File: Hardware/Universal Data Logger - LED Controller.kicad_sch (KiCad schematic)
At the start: 0 parts

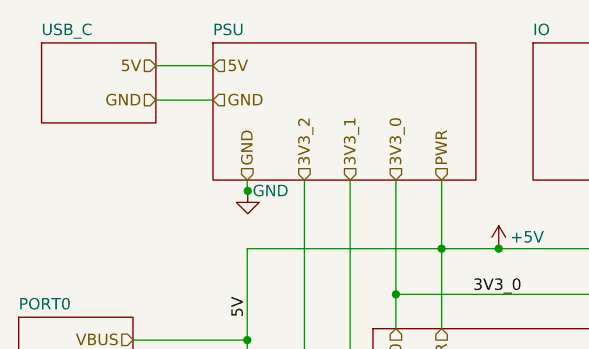
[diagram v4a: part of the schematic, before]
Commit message: added boost converter and shared power
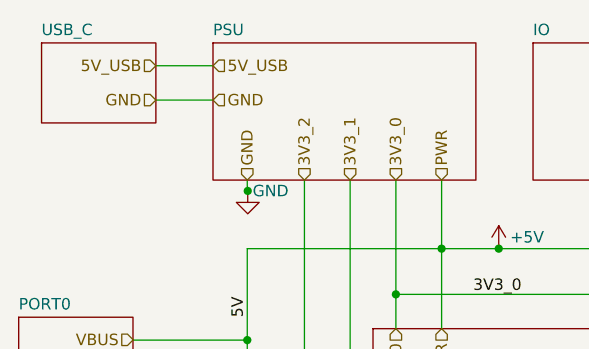
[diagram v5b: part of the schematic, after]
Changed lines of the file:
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@@
     (effects (font (size 1.27 1.27)) (justify left))
-  )
-  (hierarchical_label "5V" (shape input) (at 109.22 43.18 180)
-    (effects (font (size 1.27 1.27)) (justify right))
   )
   (hierarchical_label "3V3_0" (shape input) (at 135.89 72.39 270)
@@
     (effects (font (size 1.27 1.27)) (justify right))
   )
-  (hierarchical_label "5V" (shape input) (at 115.57 43.18 0)
+  (hierarchical_label "5V_USB" (shape input) (at 115.57 43.18 0)
     (effects (font (size 1.27 1.27)) (justify left))
   )
@@
   (hierarchical_label "3V3_0" (shape input) (at 135.89 55.88 90)
     (effects (font (size 1.27 1.27)) (justify left))
+  )
+  (hierarchical_label "5V_USB" (shape input) (at 109.22 43.18 180)
+    (effects (font (size 1.27 1.27)) (justify right))
   )
   (hierarchical_label "I2C_0" (shape input) (at 106.68 96.52 180)
@@
       (reference "#PWR?") (unit 1) (value "GND") (footprint "")
     )
+    (path "/de536fb9-bd34-41b3-aa78-3b4ee3eb44c1/816e4c72-e10d-4109-92a5-908b846ac521"
+      (reference "#PWR?") (unit 1) (value "GND") (footprint "")
+    )
     (path "/7725ee63-5a52-4ce3-8509-bb9f639adcfa/89bff7d1-eb89-4467-abd1-c6203a55d334"
       (reference "#PWR?") (unit 1) (value "~") (footprint "")
@@
       (reference "#PWR?") (unit 1) (value "GND") (footprint "")
     )
+    (path "/de536fb9-bd34-41b3-aa78-3b4ee3eb44c1/e616355e-b9c7-466d-8d6b-f6372f5c9430"
+      (reference "#PWR?") (unit 1) (value "GND") (footprint "")
+    )
     (path "/ed8d3444-b973-4b23-b52f-30b61ef22ad3"
       (reference "#PWR?") (unit 1) (value "GND") (footprint "")
@@
       (reference "#PWR?") (unit 1) (value "~") (footprint "")
     )
+    (path "/0b401b8f-2393-4525-bdd9-a0e4dc05fd07/f296a7f9-6705-4446-8a68-6cdcf5f6b1e7"
+      (reference "#PWR?") (unit 1) (value "~") (footprint "")
+    )
     (path "/416a6167-b792-4f97-9743-b5ec01ae5243/f296a7f9-6705-4446-8a68-6cdcf5f6b1e7"
-      (reference "#PWR?") (unit 1) (value "~") (footprint "")
-    )
-    (path "/0b401b8f-2393-4525-bdd9-a0e4dc05fd07/f296a7f9-6705-4446-8a68-6cdcf5f6b1e7"
       (reference "#PWR?") (unit 1) (value "~") (footprint "")
     )
@@
       (reference "C?") (unit 1) (value "10u") (footprint "")
     )
+    (path "/de536fb9-bd34-41b3-aa78-3b4ee3eb44c1/1aeb5f5f-cdff-4997-9c39-bf9eb003ca01"
+      (reference "C?") (unit 1) (value "1u") (footprint "")
+    )
+    (path "/de536fb9-bd34-41b3-aa78-3b4ee3eb44c1/1f3f4a2b-ad4c-4cfc-b60f-53aa9a5a4963"
+      (reference "C?") (unit 1) (value "10u") (footprint "")
+    )
     (path "/7c624ac6-450b-40ca-801e-524e011fb28e/31a2d955-d31f-4da0-8acb-4b0674a9da0a"
       (reference "C?") (unit 1) (value "4.7u") (footprint "")
     )
+    (path "/de536fb9-bd34-41b3-aa78-3b4ee3eb44c1/3a81c65e-eb89-462a-bf3f-509d8f776024"
+      (reference "C?") (unit 1) (value "4.7u") (footprint "")
+    )
     (path "/9782f829-68cb-4687-94a0-b365f380bc5e/3f06b84e-e0ff-4f8c-998d-4e1f029dcf28"
       (reference "C?") (unit 1) (value "10nF") (footprint "Capacitor_SMD:C_0805_2012Metric_Pad1.15x1.40mm_HandSolder")
@@
       (reference "C?") (unit 1) (value "10nF") (footprint "Capacitor_SMD:C_0805_2012Metric_Pad1.15x1.40mm_HandSolder")
     )
+    (path "/de536fb9-bd34-41b3-aa78-3b4ee3eb44c1/d2b1c201-3aa4-4a10-926d-482ef8e79ac4"
+      (reference "C?") (unit 1) (value "4.7u") (footprint "")
+    )
     (path "/de536fb9-bd34-41b3-aa78-3b4ee3eb44c1/d5744843-7628-4379-ab5c-db9cb496570f"
       (reference "C?") (unit 1) (value "10u") (footprint "")
@@
       (reference "D?") (unit 1) (value "GLED") (footprint "")
     )
+    (path "/de536fb9-bd34-41b3-aa78-3b4ee3eb44c1/625ae2c4-5527-4512-8d4e-2af0785a4a51"
+      (reference "D?") (unit 1) (value "15MQ 040NTR") (footprint "")
+    )
     (path "/9f024182-f9b7-433c-babf-5bba7b2290ff/c65fc7ad-c5d7-4502-ab26-6038cc997284"
       (reference "D?") (unit 1) (value "~") (footprint "")
@@
       (reference "J?") (unit 1) (value "~") (footprint "")
     )
+    (path "/416a6167-b792-4f97-9743-b5ec01ae5243/365bbbd0-ace9-4e3f-a9ec-01ed49158099"
+      (reference "J?") (unit 1) (value "~") (footprint "")
+    )
     (path "/0b401b8f-2393-4525-bdd9-a0e4dc05fd07/365bbbd0-ace9-4e3f-a9ec-01ed49158099"
       (reference "J?") (unit 1) (value "~") (footprint "")
     )
-    (path "/416a6167-b792-4f97-9743-b5ec01ae5243/365bbbd0-ace9-4e3f-a9ec-01ed49158099"
-      (reference "J?") (unit 1) (value "~") (footprint "")
+    (path "/de536fb9-bd34-41b3-aa78-3b4ee3eb44c1/9d457abc-74ee-43b4-89ec-b5a19bd46e46"
+      (reference "J?") (unit 1) (value "Bat_conn") (footprint "")
     )
     (path "/aa6de945-d617-4c34-aaed-6b2511874162/baf5ed95-c1f0-4125-a1c7-86f2d1455922"
@@
       (reference "L?") (unit 1) (value "BLM21PG 221") (footprint "")
     )
+    (path "/de536fb9-bd34-41b3-aa78-3b4ee3eb44c1/ff82fc8e-d594-45e1-9241-bbd7809e4925"
+      (reference "L?") (unit 1) (value "L-1616FPS 10uH") (footprint "")
+    )
+    (path "/0b401b8f-2393-4525-bdd9-a0e4dc05fd07/12f23d58-6cd8-4e91-9a7a-e2dde86f8cdc"
+      (reference "Q?") (unit 1) (value "SI4776DY-GE3") (footprint "")
+    )
     (path "/416a6167-b792-4f97-9743-b5ec01ae5243/12f23d58-6cd8-4e91-9a7a-e2dde86f8cdc"
       (reference "Q?") (unit 1) (value "SI4776DY-GE3") (footprint "")
     )
-    (path "/0b401b8f-2393-4525-bdd9-a0e4dc05fd07/12f23d58-6cd8-4e91-9a7a-e2dde86f8cdc"
-      (reference "Q?") (unit 1) (value "SI4776DY-GE3") (footprint "")
-    )
     (path "/c971c3c7-985e-4332-a313-1f1d6be5ff28/51791cbc-f8a9-4c8c-a545-ce54e428586e"
       (reference "Q?") (unit 1) (value "SI4776DY-GE3") (footprint "")
@@
       (reference "Q?") (unit 1) (value "FDN 337N") (footprint "")
     )
+    (path "/de536fb9-bd34-41b3-aa78-3b4ee3eb44c1/e8511008-8dc7-485f-ac0c-09dd4f456a12"
+      (reference "Q?") (unit 1) (value "DMP 3098L7 DII") (footprint "")
+    )
     (path "/9f024182-f9b7-433c-babf-5bba7b2290ff/f53beff6-ef87-46ca-9966-9b830c702cb4"
       (reference "Q?") (unit 1) (value "SI4776DY-GE3") (footprint "")
     )
+    (path "/de536fb9-bd34-41b3-aa78-3b4ee3eb44c1/0696e4fd-77b9-43aa-a40a-93c10a8b5533"
+      (reference "R?") (unit 1) (value "10k") (footprint "")
+    )
     (path "/9782f829-68cb-4687-94a0-b365f380bc5e/0c0a032c-edb8-4b88-97d0-bf4c00468844"
       (reference "R?") (unit 1) (value "10k") (footprint "Resistor_SMD:R_0805_2012Metric_Pad1.20x1.40mm_HandSolder")
@@
       (reference "R?") (unit 1) (value "10k") (footprint "Resistor_SMD:R_0805_2012Metric_Pad1.20x1.40mm_HandSolder")
     )
+    (path "/de536fb9-bd34-41b3-aa78-3b4ee3eb44c1/2ab9ed47-426d-4e7d-82fd-301adda43001"
+      (reference "R?") (unit 1) (value "100k") (footprint "")
+    )
     (path "/7725ee63-5a52-4ce3-8509-bb9f639adcfa/2fb8ee3f-eda6-4cc6-97f2-6249894f7413"
       (reference "R?") (unit 1) (value "~") (footprint "")
@@
       (reference "R?") (unit 1) (value "~") (footprint "")
     )
+    (path "/416a6167-b792-4f97-9743-b5ec01ae5243/5698644b-8ef8-4bcf-8ad0-1fb14fd3d883"
+      (reference "R?") (unit 1) (value "~") (footprint "")
+    )
     (path "/0b401b8f-2393-4525-bdd9-a0e4dc05fd07/5698644b-8ef8-4bcf-8ad0-1fb14fd3d883"
       (reference "R?") (unit 1) (value "~") (footprint "")
     )
-    (path "/416a6167-b792-4f97-9743-b5ec01ae5243/5698644b-8ef8-4bcf-8ad0-1fb14fd3d883"
+    (path "/416a6167-b792-4f97-9743-b5ec01ae5243/5bd76eea-534b-467c-9a4a-7dca5914f664"
       (reference "R?") (unit 1) (value "~") (footprint "")
     )
     (path "/0b401b8f-2393-4525-bdd9-a0e4dc05fd07/5bd76eea-534b-467c-9a4a-7dca5914f664"
-      (reference "R?") (unit 1) (value "~") (footprint "")
-    )
-    (path "/416a6167-b792-4f97-9743-b5ec01ae5243/5bd76eea-534b-467c-9a4a-7dca5914f664"
       (reference "R?") (unit 1) (value "~") (footprint "")
     )
@@
       (reference "R?") (unit 1) (value "1k") (footprint "")
     )
+    (path "/de536fb9-bd34-41b3-aa78-3b4ee3eb44c1/b2083824-9588-40f5-89d7-35aa52c6eaff"
+      (reference "R?") (unit 1) (value "976k") (footprint "")
+    )
     (path "/9f024182-f9b7-433c-babf-5bba7b2290ff/b9ba3eb3-9074-471c-8f12-7ba4ff7a66f6"
       (reference "R?") (unit 1) (value "~") (footprint "")
@@
       (reference "R?") (unit 1) (value "10k") (footprint "Resistor_SMD:R_0805_2012Metric_Pad1.20x1.40mm_HandSolder")
     )
+    (path "/de536fb9-bd34-41b3-aa78-3b4ee3eb44c1/e800ee31-5b2a-4aab-bd1b-996c17c6f049"
+      (reference "R?") (unit 1) (value "309k") (footprint "")
+    )
     (path "/9782f829-68cb-4687-94a0-b365f380bc5e/103ba368-d824-4319-941a-bc4167f5eb02"
       (reference "SW?") (unit 1) (value "Rotary_Encoder") (footprint "Rotary_Encoder:RotaryEncoder_Alps_EC12E-Switch_Vertical_H20mm")
@@
       (reference "U?") (unit 1) (value "AP1117-33") (footprint "Package_TO_SOT_SMD:SOT-223-3_TabPin2")
     )
+    (path "/de536fb9-bd34-41b3-aa78-3b4ee3eb44c1/8affedf3-2c25-40d4-96c3-bb27a68a6d1e"
+      (reference "U?") (unit 1) (value "MCP1640CH") (footprint "Package_TO_SOT_SMD:SOT-23-6")
+    )
     (path "/de536fb9-bd34-41b3-aa78-3b4ee3eb44c1/8f8f9a7d-5e85-4d25-bc41-68f36698606e"
       (reference "U?") (unit 1) (value "AP1117-33") (footprint "Package_TO_SOT_SMD:SOT-223-3_TabPin2")
@@
       (reference "U?") (unit 1) (value "ESP32-S2-WROVER") (footprint "RF_Module:ESP32-S2-WROVER")
     )
-  )
+    (path "/de536fb9-bd34-41b3-aa78-3b4ee3eb44c1/9bd027c7-d1af-4bc6-a88c-88f4204bfad0"
+      (reference "U?") (unit 1) (value "MCP73831-2-OT") (footprint "Package_TO_SOT_SMD:SOT-23-5")
+    )
+  )

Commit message: fixes for hierarchical sheets
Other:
- sheet PORT0 ports: added EN, I2C_0; removed none
- sheet PSU ports: added 3V3_0, 3V3_1, 3V3_2, 5V_USB, PWR, bat_sense; removed none
- sheet USB_C ports: added 5V_USB; removed none

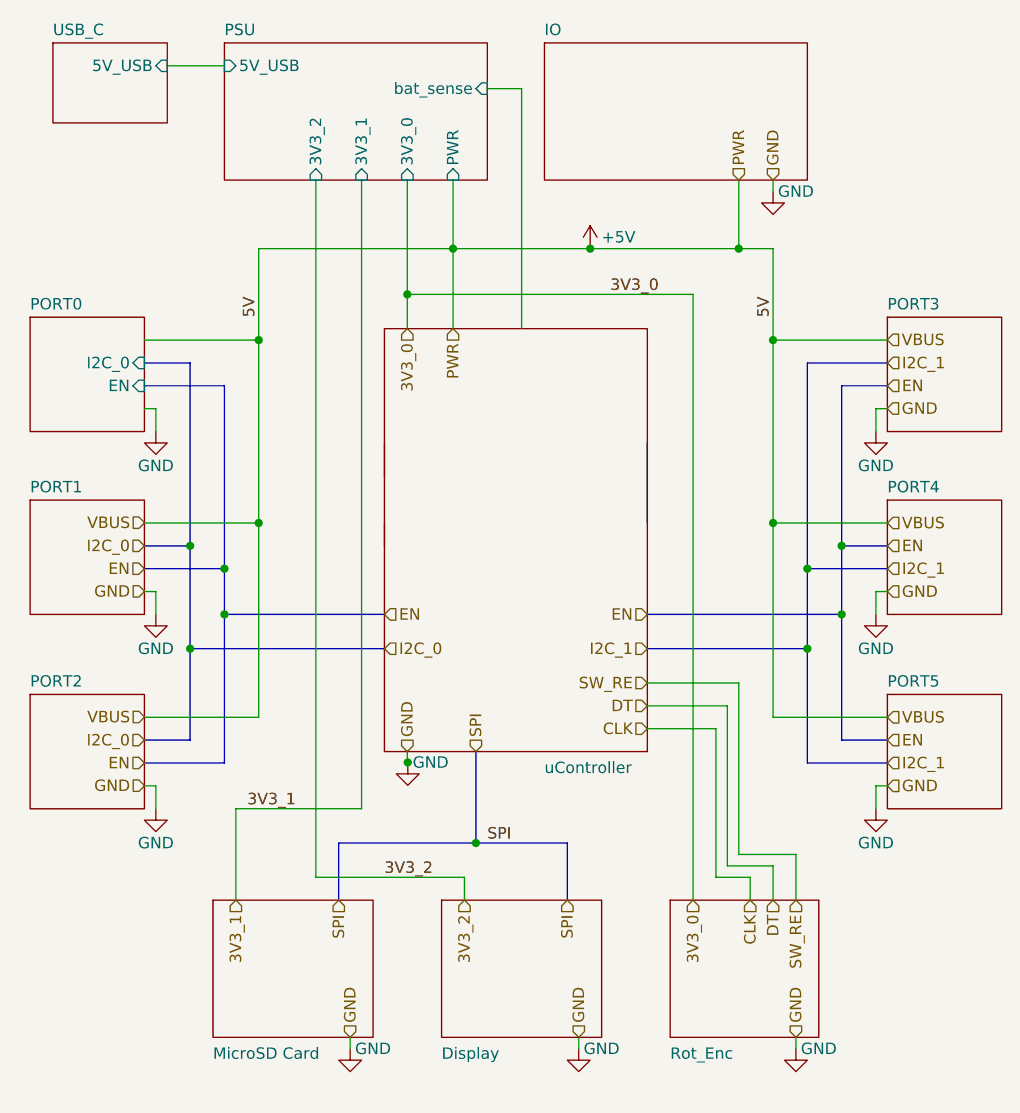
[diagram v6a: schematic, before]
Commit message: added hierrarchial labels
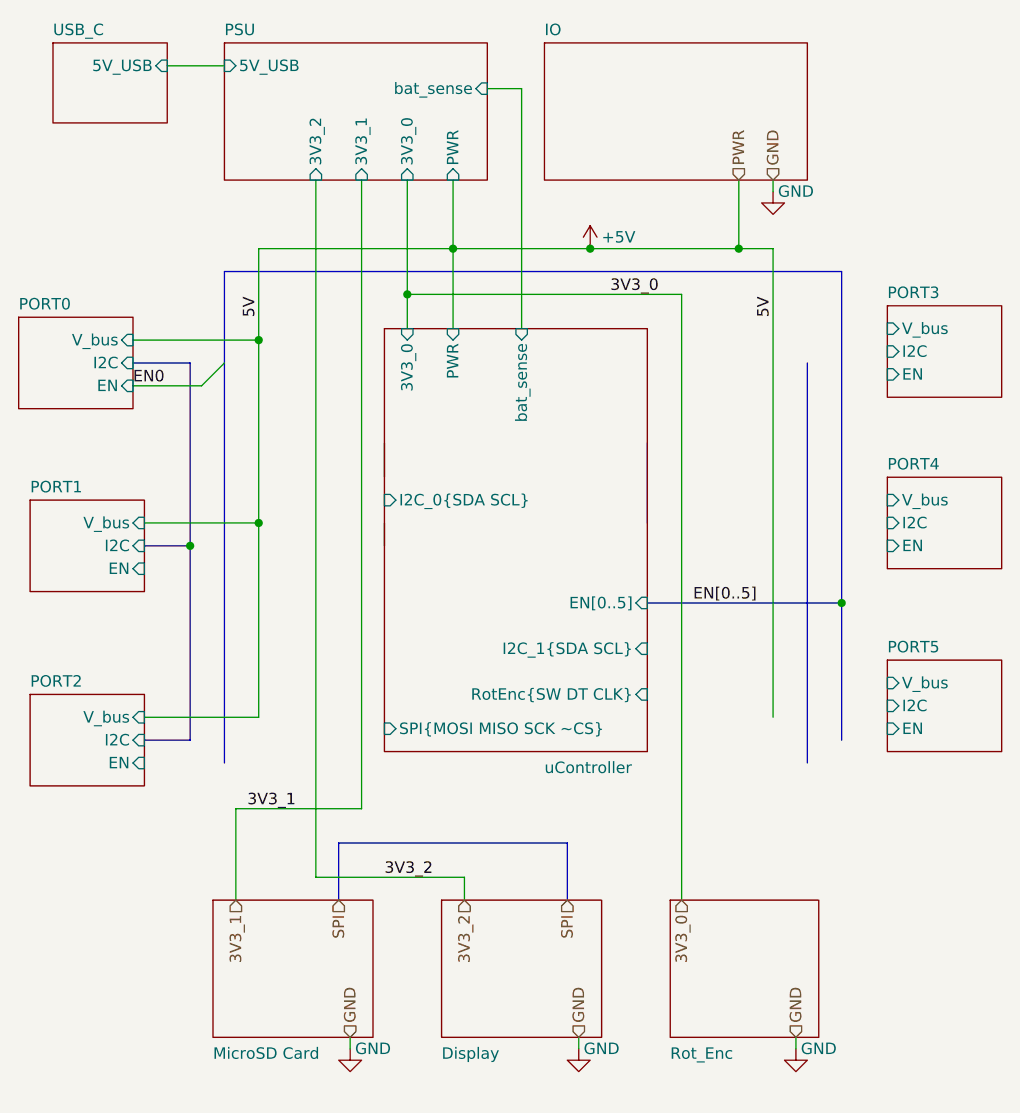
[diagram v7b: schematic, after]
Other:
- sheet PORT0: file PORT0.kicad_sch -> PORT.kicad_sch
- sheet PORT0 ports: added I2C, V_bus; removed I2C_0
- sheet PORT1: file PORT1.kicad_sch -> PORT.kicad_sch
- sheet PORT1 ports: added EN, I2C, V_bus; removed none
- sheet PORT2: file PORT2.kicad_sch -> PORT.kicad_sch
- sheet PORT2 ports: added EN, I2C, V_bus; removed none
- sheet PORT3: file PORT3.kicad_sch -> PORT.kicad_sch
- sheet PORT3 ports: added EN, I2C, V_bus; removed none
- sheet PORT4: file PORT4.kicad_sch -> PORT.kicad_sch
- sheet PORT4 ports: added EN, I2C, V_bus; removed none
- sheet PORT5: file PORT5.kicad_sch -> PORT.kicad_sch
- sheet PORT5 ports: added EN, I2C, V_bus; removed none
- sheet uController ports: added 3V3_0, EN[0..5], I2C_0{SDA SCL}, I2C_1{SDA SCL}, PWR, RotEnc{SW DT CLK}, SPI{MOSI MISO SCK ~CS}, bat_sense; removed none

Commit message: cleaned up busses
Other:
- sheet Display ports: added 3V3, SPI{MOSI MISO SCK ~{CS}}; removed none
- sheet MicroSD Card ports: added 3V3, SPI{MOSI MISO SCK ~{CS}}; removed none
- sheet PORT0 ports: added SCL, SDA; removed I2C
- sheet PORT1 ports: added SCL, SDA; removed I2C
- sheet PORT2 ports: added SCL, SDA; removed I2C
- sheet PORT3 ports: added SCL, SDA; removed I2C
- sheet PORT4 ports: added SCL, SDA; removed I2C
- sheet PORT5 ports: added SCL, SDA; removed I2C
- sheet Rot_Enc ports: added 3V3, RotEnc{SW DT CLK}; removed none
- sheet uController ports: added 3V3, SPI{MOSI MISO SCK ~{CS}}; removed 3V3_0, SPI{MOSI MISO SCK ~CS}
